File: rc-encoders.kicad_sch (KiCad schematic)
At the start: 20 parts

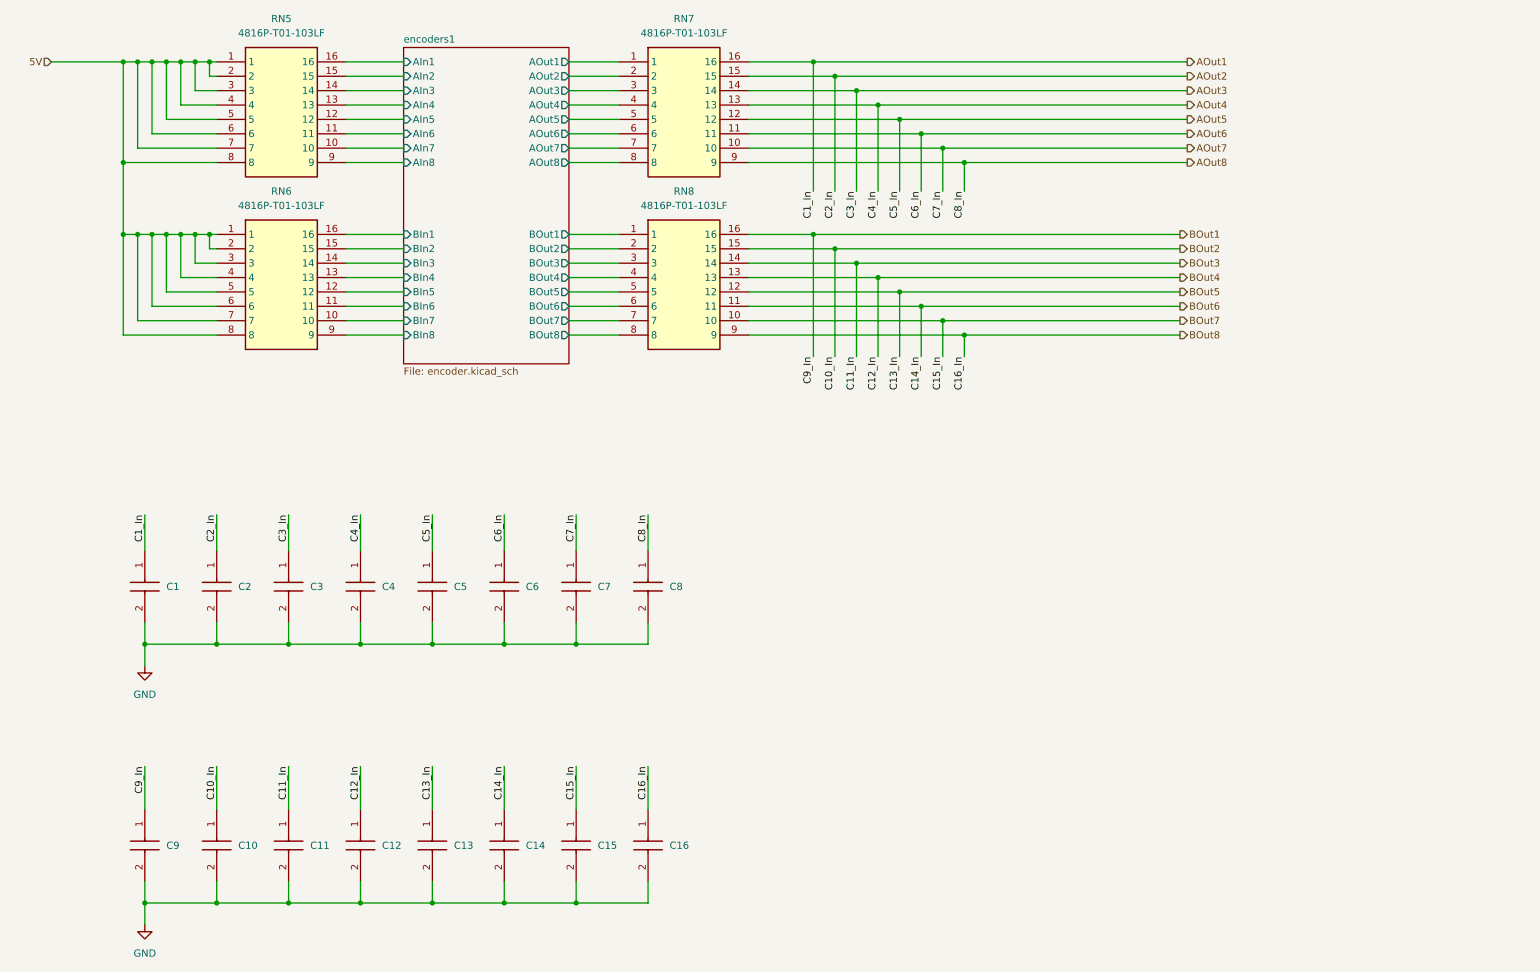
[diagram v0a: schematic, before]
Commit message: Added rest of the encoder terminal to hierarchical sheets
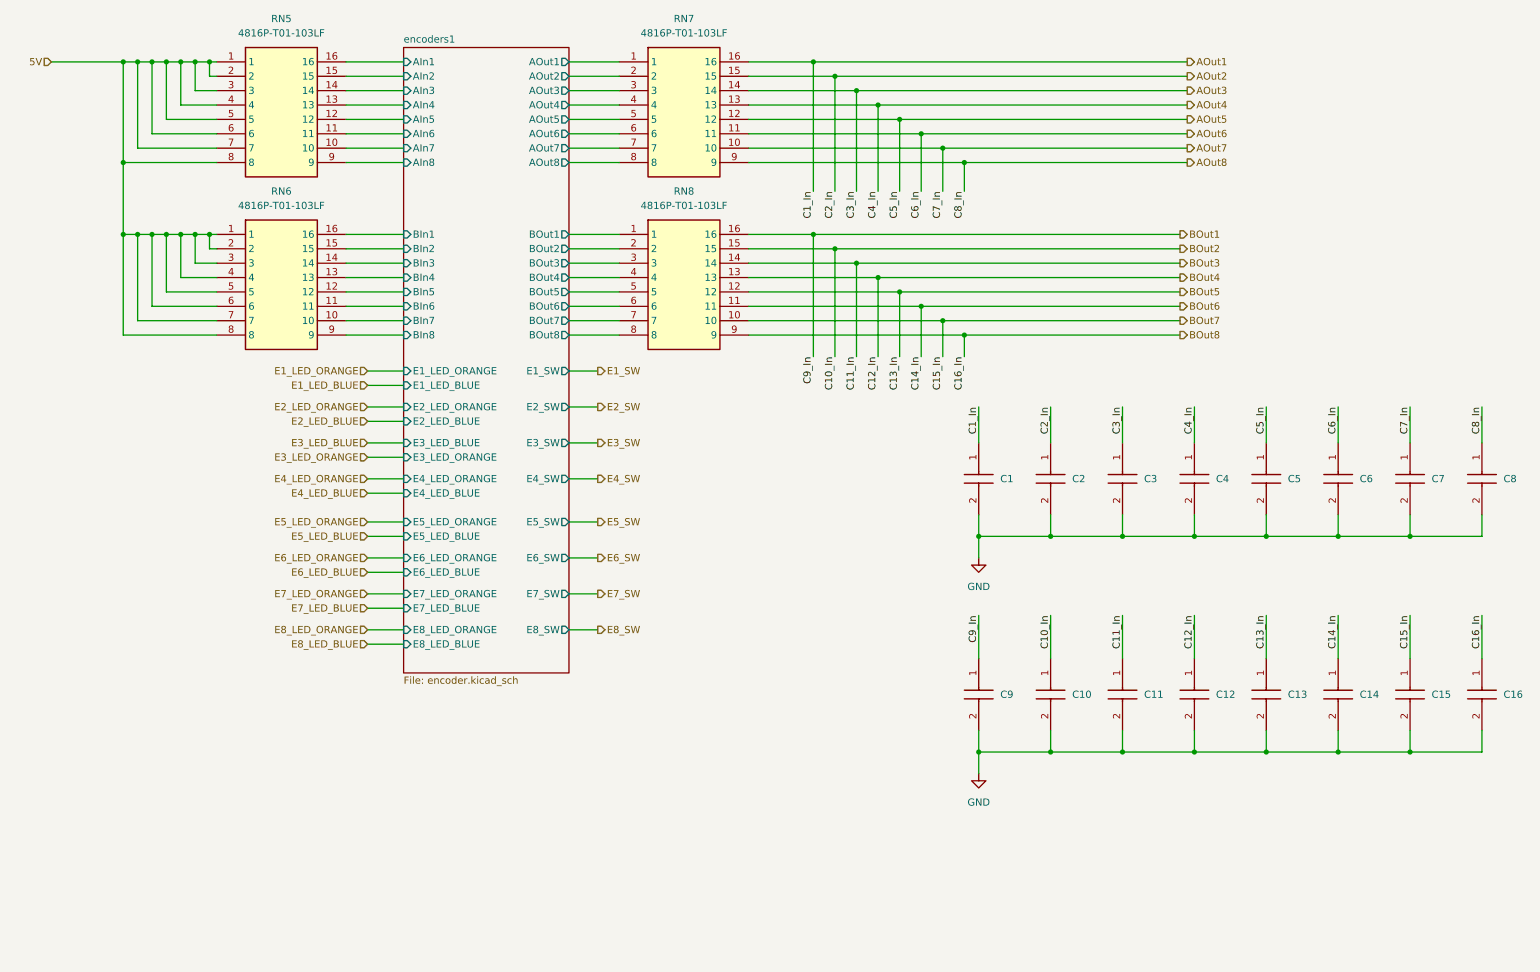
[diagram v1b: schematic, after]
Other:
- sheet encoders1 ports: added E1_LED_BLUE, E1_LED_ORANGE, E1_SW, E2_LED_BLUE, E2_LED_ORANGE, E2_SW, E3_LED_BLUE, E3_LED_ORANGE, E3_SW, E4_LED_BLUE, E4_LED_ORANGE, E4_SW, E5_LED_BLUE, E5_LED_ORANGE, E5_SW, E6_LED_BLUE, E6_LED_ORANGE, E6_SW, E7_LED_BLUE, E7_LED_ORANGE, E7_SW, E8_LED_BLUE, E8_LED_ORANGE, E8_SW; removed none
- moved on the sheet: C1, C10, C11, C12, C13, C14, C15, C16, C2, C3, C4, C5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

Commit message: Update schematic
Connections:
- net 5V renamed 3.3V
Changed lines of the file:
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@@
 		)
 	)
-	(hierarchical_label "5V"
+	(hierarchical_label "3.3V"
 		(shape input)
 		(at 22.86 30.48 180)

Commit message: Made fixes according to the erc
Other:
- sheet encoders1 ports: added none; removed E1_SW, E2_SW, E3_SW, E4_SW, E5_SW, E6_SW, E7_SW, E8_SW
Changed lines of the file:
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@@
 	(wire
 		(pts
-			(xy 119.38 104.14) (xy 114.3 104.14)
-		)
-		(stroke
-			(width 0)
-			(type default)
-		)
-	)
-	(wire
-		(pts
 			(xy 78.74 97.79) (xy 85.09 97.79)
 		)
@@
 	(wire
 		(pts
-			(xy 119.38 111.76) (xy 114.3 111.76)
-		)
-		(stroke
-			(width 0)
-			(type default)
-		)
-	)
-	(wire
-		(pts
 			(xy 22.86 30.48) (xy 35.56 30.48)
 		)
@@
 	(wire
 		(pts
-			(xy 119.38 124.46) (xy 114.3 124.46)
-		)
-		(stroke
-			(width 0)
-			(type default)
-		)
-	)
-	(wire
-		(pts
 			(xy 184.15 48.26) (xy 223.52 48.26)
 		)
@@
 	(wire
 		(pts
-			(xy 119.38 91.44) (xy 114.3 91.44)
-		)
-		(stroke
-			(width 0)
-			(type default)
-		)
-	)
-	(wire
-		(pts
 			(xy 180.34 76.2) (xy 222.25 76.2)
 		)
@@
 	(wire
 		(pts
-			(xy 119.38 118.11) (xy 114.3 118.11)
-		)
-		(stroke
-			(width 0)
-			(type default)
-		)
-	)
-	(wire
-		(pts
 			(xy 78.74 133.35) (xy 85.09 133.35)
 		)
@@
 	(wire
 		(pts
-			(xy 119.38 97.79) (xy 114.3 97.79)
-		)
-		(stroke
-			(width 0)
-			(type default)
-		)
-	)
-	(wire
-		(pts
 			(xy 168.91 68.58) (xy 168.91 82.55)
 		)
@@
 	(wire
 		(pts
-			(xy 119.38 130.81) (xy 114.3 130.81)
-		)
-		(stroke
-			(width 0)
-			(type default)
-		)
-	)
-	(wire
-		(pts
 			(xy 161.29 63.5) (xy 222.25 63.5)
 		)
@@
 	(wire
 		(pts
-			(xy 119.38 85.09) (xy 114.3 85.09)
-		)
-		(stroke
-			(width 0)
-			(type default)
-		)
-	)
-	(wire
-		(pts
 			(xy 186.69 114.3) (xy 186.69 118.11)
 		)
@@
 		)
 	)
-	(hierarchical_label "E7_SW"
-		(shape output)
-		(at 119.38 124.46 0)
-		(effects
-			(font
-				(size 1.27 1.27)
-			)
-			(justify left)
-		)
-	)
-	(hierarchical_label "E3_SW"
-		(shape output)
-		(at 119.38 97.79 0)
-		(effects
-			(font
-				(size 1.27 1.27)
-			)
-			(justify left)
-		)
-	)
 	(hierarchical_label "E5_LED_ORANGE"
 		(shape input)
@@
 		)
 	)
-	(hierarchical_label "E8_SW"
-		(shape output)
-		(at 119.38 130.81 0)
-		(effects
-			(font
-				(size 1.27 1.27)
-			)
-			(justify left)
-		)
-	)
 	(hierarchical_label "AOut2"
 		(shape output)
@@
 		)
 	)
-	(hierarchical_label "E4_SW"
-		(shape output)
-		(at 119.38 104.14 0)
-		(effects
-			(font
-				(size 1.27 1.27)
-			)
-			(justify left)
-		)
-	)
 	(hierarchical_label "BOut6"
 		(shape output)
@@
 		)
 	)
-	(hierarchical_label "E5_SW"
-		(shape output)
-		(at 119.38 111.76 0)
-		(effects
-			(font
-				(size 1.27 1.27)
-			)
-			(justify left)
-		)
-	)
-	(hierarchical_label "E1_SW"
-		(shape output)
-		(at 119.38 85.09 0)
-		(effects
-			(font
-				(size 1.27 1.27)
-			)
-			(justify left)
-		)
-	)
 	(hierarchical_label "AOut3"
 		(shape output)
@@
 		)
 	)
-	(hierarchical_label "E2_SW"
-		(shape output)
-		(at 119.38 91.44 0)
-		(effects
-			(font
-				(size 1.27 1.27)
-			)
-			(justify left)
-		)
-	)
-	(hierarchical_label "E6_SW"
-		(shape output)
-		(at 119.38 118.11 0)
-		(effects
-			(font
-				(size 1.27 1.27)
-			)
-			(justify left)
-		)
-	)
 	(hierarchical_label "AOut4"
 		(shape output)
@@
 			)
 		)
-		(pin "E1_SW" output
-			(at 114.3 85.09 0)
-			(effects
-				(font
-					(size 1.27 1.27)
-				)
-				(justify right)
-			)
-		)
 		(pin "E1_LED_BLUE" input
 			(at 85.09 87.63 180)
@@
 			)
 		)
-		(pin "E2_SW" output
-			(at 114.3 91.44 0)
-			(effects
-				(font
-					(size 1.27 1.27)
-				)
-				(justify right)
-			)
-		)
 		(pin "E3_LED_BLUE" input
 			(at 85.09 97.79 180)
@@
 			)
 		)
-		(pin "E3_SW" output
-			(at 114.3 97.79 0)
-			(effects
-				(font
-					(size 1.27 1.27)
-				)
-				(justify right)
-			)
-		)
 		(pin "E4_LED_ORANGE" input
 			(at 85.09 104.14 180)
@@
 			)
 		)
-		(pin "E4_SW" output
-			(at 114.3 104.14 0)
-			(effects
-				(font
-					(size 1.27 1.27)
-				)
-				(justify right)
-			)
-		)
-		(pin "E5_SW" output
-			(at 114.3 111.76 0)
-			(effects
-				(font
-					(size 1.27 1.27)
-				)
-				(justify right)
-			)
-		)
 		(pin "E5_LED_ORANGE" input
 			(at 85.09 111.76 180)
@@
 			)
 		)
-		(pin "E6_SW" output
-			(at 114.3 118.11 0)
-			(effects
-				(font
-					(size 1.27 1.27)
-				)
-				(justify right)
-			)
-		)
 		(pin "E7_LED_ORANGE" input
 			(at 85.09 124.46 180)
@@
 			)
 		)
-		(pin "E7_SW" output
-			(at 114.3 124.46 0)
-			(effects
-				(font
-					(size 1.27 1.27)
-				)
-				(justify right)
-			)
-		)
 		(pin "E8_LED_ORANGE" input
 			(at 85.09 130.81 180)
@@
 			)
 		)
-		(pin "E8_SW" output
-			(at 114.3 130.81 0)
-			(effects
-				(font
-					(size 1.27 1.27)
-				)
-				(justify right)
-			)
-		)

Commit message: PCB Ready
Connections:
- net encoders1/AOut1 is gone; now on net encoders1/AIn1: RN7.1
- net encoders1/AOut2 is gone; now on net encoders1/AIn2: RN7.2
- net encoders1/AOut3 is gone; now on net encoders1/AIn3: RN7.3
- net encoders1/AOut4 is gone; now on net encoders1/AIn4: RN7.4
- net encoders1/AOut5 is gone; now on net encoders1/AIn5: RN7.5
- net encoders1/AOut6 is gone; now on net encoders1/AIn6: RN7.6
- net encoders1/AOut7 is gone; now on net encoders1/AIn7: RN7.7
- net encoders1/AOut8 is gone; now on net encoders1/AIn8: RN7.8
- net encoders1/BOut1 is gone; now on net encoders1/BIn1: RN8.1
- net encoders1/BOut2 is gone; now on net encoders1/BIn2: RN8.2
- net encoders1/BOut3 is gone; now on net encoders1/BIn3: RN8.3
- net encoders1/BOut4 is gone; now on net encoders1/BIn4: RN8.4
- net encoders1/BOut5 is gone; now on net encoders1/BIn5: RN8.5
- net encoders1/BOut6 is gone; now on net encoders1/BIn6: RN8.6
- net encoders1/BOut7 is gone; now on net encoders1/BIn7: RN8.7
- net encoders1/BOut8 is gone; now on net encoders1/BIn8: RN8.8
- net AOut1 renamed A_Out1
- net AOut2 renamed A_Out2
- net AOut3 renamed A_Out3
- net AOut4 renamed A_Out4
- net AOut5 renamed A_Out5
- net AOut6 renamed A_Out6
- net AOut7 renamed A_Out7
- net AOut8 renamed A_Out8
- net BOut1 renamed B_Out1
- net BOut2 renamed B_Out2
- net BOut3 renamed B_Out3
- net BOut4 renamed B_Out4
- net BOut5 renamed B_Out5
- net BOut6 renamed B_Out6
- net BOut7 renamed B_Out7
- net BOut8 renamed B_Out8
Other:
- sheet encoders1 ports: added none; removed AOut1, AOut2, AOut3, AOut4, AOut5, AOut6, AOut7, AOut8, BOut1, BOut2, BOut3, BOut4, BOut5, BOut6, BOut7, BOut8
- moved on the sheet: C1, C10, C11, C12, C13, C14, C15, C16, C2, C3, C4, C5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
